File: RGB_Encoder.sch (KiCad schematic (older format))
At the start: 26 parts

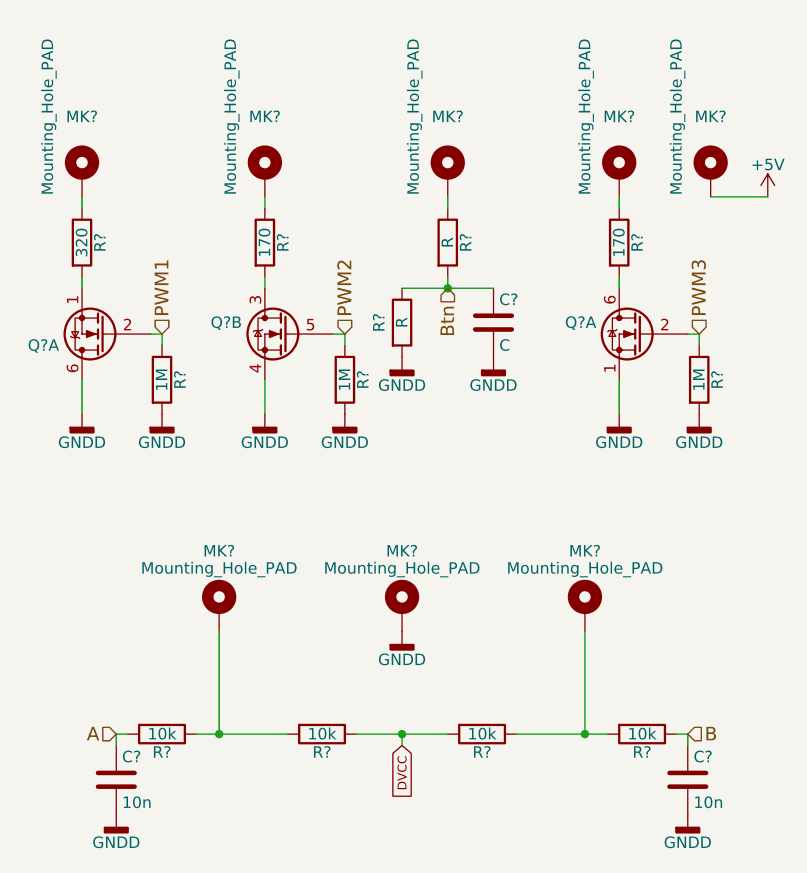
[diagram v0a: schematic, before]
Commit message: Finished Rev1 schematic and assigned most footprints
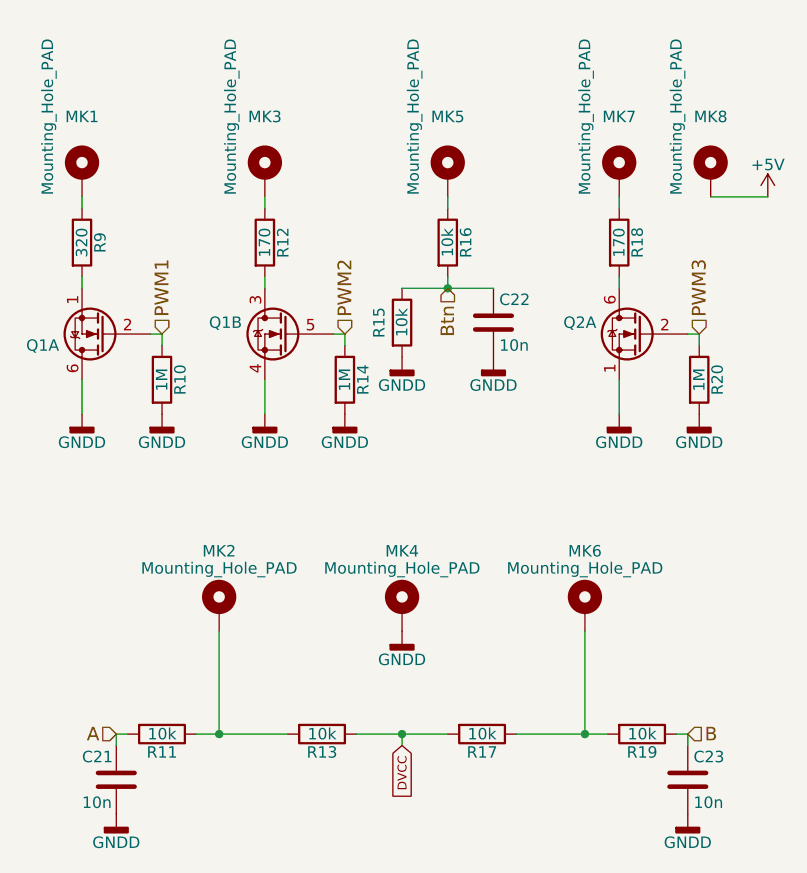
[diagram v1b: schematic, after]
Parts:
- C21, C23: renamed from C?; footprint (none) -> Capacitors_SMD:C_0603
- C22: renamed from C?; value C -> 10n; footprint (none) -> Capacitors_SMD:C_0603
- MK1, MK2, MK3, MK4, MK5, MK6, MK7, MK8: renamed from MK?; footprint (none) -> Wire_Pads:SolderWirePad_single_1mmDrill
- Q1, Q2: renamed from Q?; footprint (none) -> TO_SOT_Packages_SMD:SOT-363_SC-70-6
- R10, R11, R12, R13, R14, R17, R18, R19, R20, R9: renamed from R?; footprint (none) -> Resistors_SMD:R_0603
- R15, R16: renamed from R?; value R -> 10k; footprint (none) -> Resistors_SMD:R_0603
